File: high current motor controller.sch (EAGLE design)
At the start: 44 parts, among them Q1 IPT004N03L, Q2 IPT004N03L, Q3 IPT004N03L, Q4 IPT004N03L

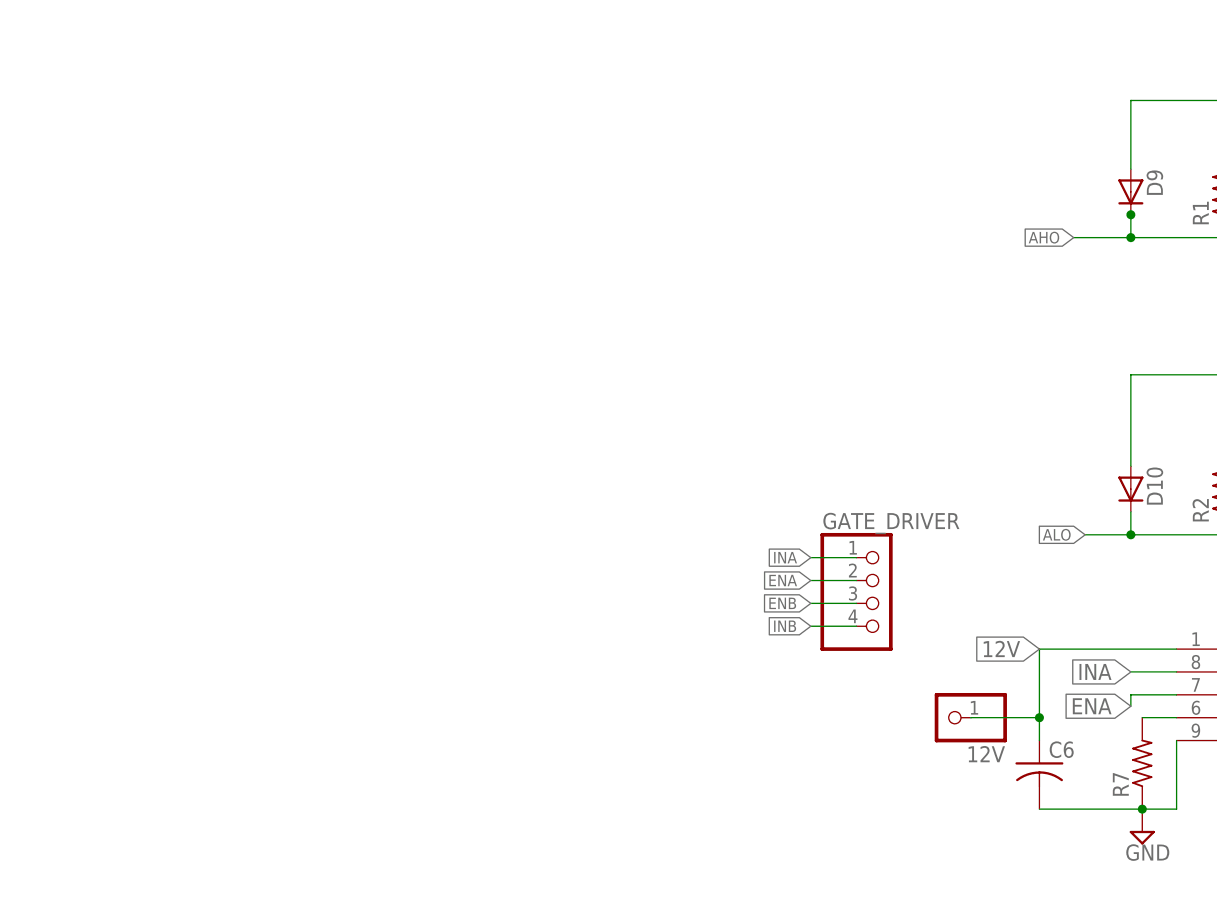
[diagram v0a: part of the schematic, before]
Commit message: Add switching regulator to transform battery voltage to 12V
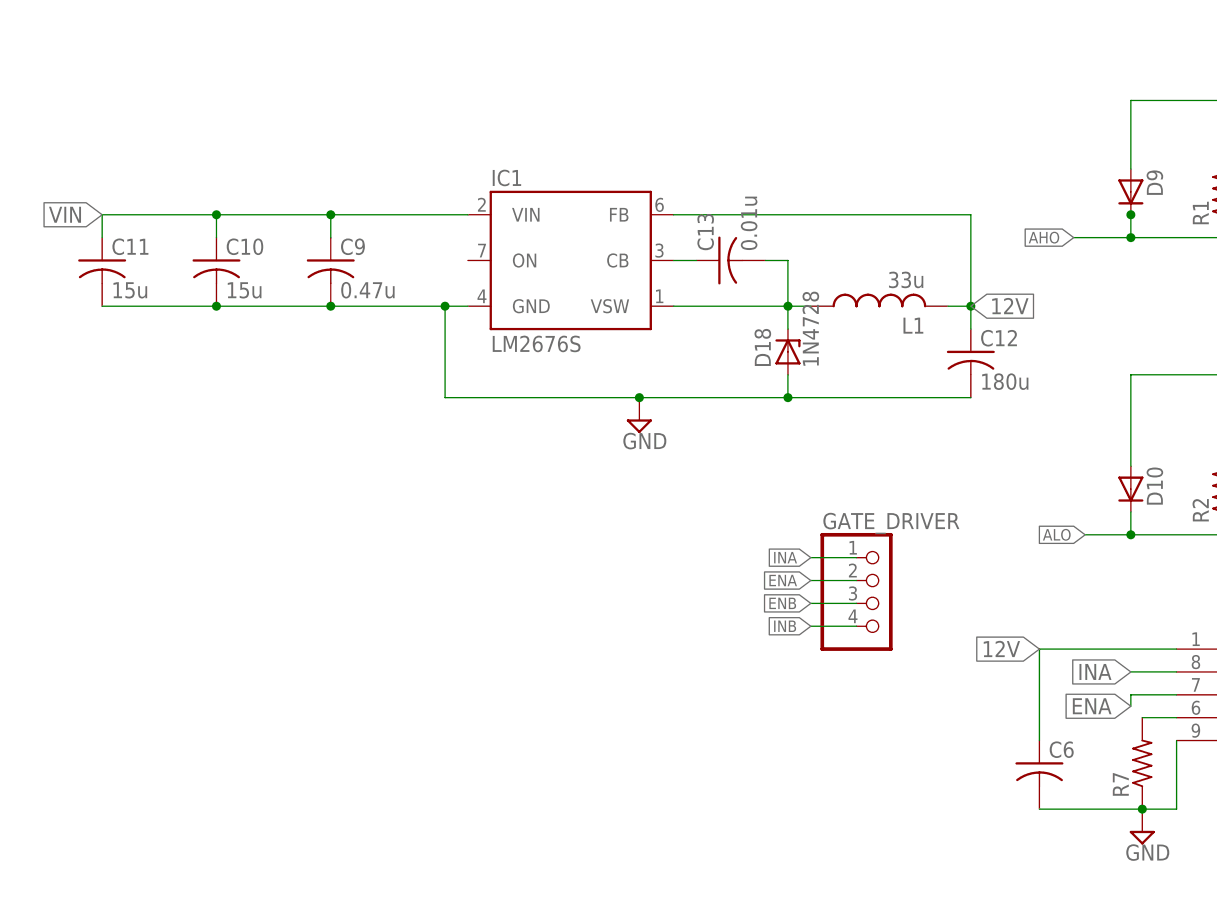
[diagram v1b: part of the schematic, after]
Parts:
- removed 12V: (no value), pinhead:PINHD-1X1
- added C10, C11: 15u, resistor:C-USC0805
- added C12: 180u, resistor:C-USC0805
- added C13: 0.01u, resistor:C-USC0805
- added C9: 0.47u, resistor:C-USC0805
- added D18: 1N4728, diode:1N4728
- added IC1: LM2676S, v-reg-3:LM2676S
- added L1: 33u, resistor:L-USL1812
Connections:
- new net N$16: C13.1, IC1.CB
- new net N$17: C13.2, D18.C, IC1.VSW, L1.1
- net 12V: now also C12.1, IC1.FB, L1.2; no longer 12V.1
- net GND: now also C10.2, C11.2, C12.2, C9.2, D18.A, IC1.GND
- net VIN: now also C10.1, C11.1, C9.1, IC1.VIN
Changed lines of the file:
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@@
 <layer number="207" name="207bmp" color="8" fill="10" visible="yes" active="yes"/>
 <layer number="208" name="208bmp" color="9" fill="10" visible="yes" active="yes"/>
+<layer number="231" name="Eagle3D_PG1" color="7" fill="1" visible="yes" active="yes"/>
+<layer number="232" name="Eagle3D_PG2" color="7" fill="1" visible="yes" active="yes"/>
+<layer number="233" name="Eagle3D_PG3" color="7" fill="1" visible="yes" active="yes"/>
 <layer number="250" name="Descript" color="3" fill="1" visible="no" active="no"/>
 <layer number="251" name="SMDround" color="12" fill="11" visible="no" active="no"/>
@@
 <part name="D17" library="diode" deviceset="GF1" device=""/>
 <part name="SUPPLY4" library="supply2" deviceset="GND" device=""/>
-<part name="12V" library="pinhead" deviceset="PINHD-1X1" device=""/>
 <part name="GATE_DRIVER" library="pinhead" deviceset="PINHD-1X4" device=""/>
 <part name="BATT_POWER" library="pinhead" deviceset="PINHD-1X3" device=""/>
+<part name="IC1" library="v-reg-3" deviceset="LM2676" device="S"/>
+<part name="C9" library="resistor" deviceset="C-US" device="C0805" value="0.47u"/>
+<part name="C10" library="resistor" deviceset="C-US" device="C0805" value="15u"/>
+<part name="C11" library="resistor" deviceset="C-US" device="C0805" value="15u"/>
+<part name="C12" library="resistor" deviceset="C-US" device="C0805" value="180u"/>
+<part name="C13" library="resistor" deviceset="C-US" device="C0805" value="0.01u"/>
+<part name="L1" library="resistor" deviceset="L-US" device="L1812" value="33u"/>
+<part name="D18" library="diode" deviceset="1N4728" device=""/>
+<part name="SUPPLY5" library="supply2" deviceset="GND" device=""/>
 </parts>
 <sheets>
@@
 <instance part="D17" gate="D" x="139.7" y="-2.54" rot="R270"/>
 <instance part="SUPPLY4" gate="GND" x="91.44" y="-27.94"/>
-<instance part="12V" gate="G$1" x="-10.16" y="-12.7" rot="R180"/>
 <instance part="GATE_DRIVER" gate="A" x="-17.78" y="0"/>
 <instance part="BATT_POWER" gate="A" x="111.76" y="78.74"/>
+<instance part="IC1" gate="A" x="-53.34" y="38.1"/>
+<instance part="C9" gate="G$1" x="-78.74" y="38.1"/>
+<instance part="C10" gate="G$1" x="-91.44" y="38.1"/>
+<instance part="C11" gate="G$1" x="-104.14" y="38.1"/>
+<instance part="C12" gate="G$1" x="-7.62" y="27.94"/>
+<instance part="C13" gate="G$1" x="-35.56" y="38.1" rot="R90"/>
+<instance part="L1" gate="G$1" x="-17.78" y="33.02" rot="R90"/>
+<instance part="D18" gate="1" x="-27.94" y="27.94" rot="R90"/>
+<instance part="SUPPLY5" gate="GND" x="-44.45" y="20.32"/>
 </instances>
 <busses>
@@
 <label x="104.14" y="76.2" size="1.27" layer="95" rot="R180" xref="yes"/>
 </segment>
+<segment>
+<pinref part="C11" gate="G$1" pin="2"/>
+<pinref part="IC1" gate="A" pin="GND"/>
+<wire x1="-104.14" y1="33.02" x2="-91.44" y2="33.02" width="0.1524" layer="91"/>
+<pinref part="C10" gate="G$1" pin="2"/>
+<wire x1="-91.44" y1="33.02" x2="-78.74" y2="33.02" width="0.1524" layer="91"/>
+<junction x="-91.44" y="33.02"/>
+<pinref part="C9" gate="G$1" pin="2"/>
+<wire x1="-78.74" y1="33.02" x2="-66.04" y2="33.02" width="0.1524" layer="91"/>
+<junction x="-78.74" y="33.02"/>
+<pinref part="C12" gate="G$1" pin="2"/>
+<wire x1="-66.04" y1="33.02" x2="-63.5" y2="33.02" width="0.1524" layer="91"/>
+<wire x1="-7.62" y1="22.86" x2="-27.94" y2="22.86" width="0.1524" layer="91"/>
+<wire x1="-27.94" y1="22.86" x2="-44.45" y2="22.86" width="0.1524" layer="91"/>
+<wire x1="-44.45" y1="22.86" x2="-66.04" y2="22.86" width="0.1524" layer="91"/>
+<wire x1="-66.04" y1="22.86" x2="-66.04" y2="33.02" width="0.1524" layer="91"/>
+<junction x="-66.04" y="33.02"/>
+<pinref part="D18" gate="1" pin="A"/>
+<wire x1="-27.94" y1="25.4" x2="-27.94" y2="22.86" width="0.1524" layer="91"/>
+<junction x="-27.94" y="22.86"/>
+<pinref part="SUPPLY5" gate="GND" pin="GND"/>
+<junction x="-44.45" y="22.86"/>
+</segment>
 </net>
 <net name="12V" class="0">
@@
 <wire x1="15.24" y1="-5.08" x2="0" y2="-5.08" width="0.1524" layer="91"/>
 <pinref part="C6" gate="G$1" pin="1"/>
-<wire x1="0" y1="-5.08" x2="0" y2="-12.7" width="0.1524" layer="91"/>
+<wire x1="0" y1="-5.08" x2="0" y2="-15.24" width="0.1524" layer="91"/>
 <label x="0" y="-5.08" size="1.778" layer="95" rot="R180" xref="yes"/>
-<pinref part="12V" gate="G$1" pin="1"/>
-<wire x1="0" y1="-12.7" x2="0" y2="-15.24" width="0.1524" layer="91"/>
-<wire x1="-7.62" y1="-12.7" x2="0" y2="-12.7" width="0.1524" layer="91"/>
-<junction x="0" y="-12.7"/>
 </segment>
 <segment>
@@
 <wire x1="139.7" y1="2.54" x2="138.43" y2="2.54" width="0.1524" layer="91"/>
 <label x="138.43" y="2.54" size="1.778" layer="95" rot="R180" xref="yes"/>
+</segment>
+<segment>
+<pinref part="L1" gate="G$1" pin="2"/>
+<pinref part="C12" gate="G$1" pin="1"/>
+<wire x1="-10.16" y1="33.02" x2="-7.62" y2="33.02" width="0.1524" layer="91"/>
+<wire x1="-7.62" y1="33.02" x2="-7.62" y2="30.48" width="0.1524" layer="91"/>
+<pinref part="IC1" gate="A" pin="FB"/>
+<wire x1="-7.62" y1="33.02" x2="-7.62" y2="43.18" width="0.1524" layer="91"/>
+<wire x1="-7.62" y1="43.18" x2="-40.64" y2="43.18" width="0.1524" layer="91"/>
+<junction x="-7.62" y="33.02"/>
+<label x="-7.62" y="33.02" size="1.778" layer="95" xref="yes"/>
 </segment>
 </net>
@@
 <label x="104.14" y="81.28" size="1.27" layer="95" rot="R180" xref="yes"/>
 </segment>
-</net>
+<segment>
+<pinref part="IC1" gate="A" pin="VIN"/>
+<pinref part="C11" gate="G$1" pin="1"/>
+<wire x1="-63.5" y1="43.18" x2="-78.74" y2="43.18" width="0.1524" layer="91"/>
+<wire x1="-78.74" y1="43.18" x2="-91.44" y2="43.18" width="0.1524" layer="91"/>
+<wire x1="-91.44" y1="43.18" x2="-104.14" y2="43.18" width="0.1524" layer="91"/>
+<wire x1="-104.14" y1="43.18" x2="-104.14" y2="40.64" width="0.1524" layer="91"/>
+<pinref part="C10" gate="G$1" pin="1"/>
+<wire x1="-91.44" y1="40.64" x2="-91.44" y2="43.18" width="0.1524" layer="91"/>
+<junction x="-91.44" y="43.18"/>
+<pinref part="C9" gate="G$1" pin="1"/>
+<wire x1="-78.74" y1="40.64" x2="-78.74" y2="43.18" width="0.1524" layer="91"/>
+<junction x="-78.74" y="43.18"/>
+<label x="-104.14" y="43.18" size="1.778" layer="95" rot="R180" xref="yes"/>
+</segment>
+</net>
+<net name="N$16" class="0">
+<segment>
+<pinref part="IC1" gate="A" pin="CB"/>
+<pinref part="C13" gate="G$1" pin="1"/>
+<wire x1="-38.1" y1="38.1" x2="-40.64" y2="38.1" width="0.1524" layer="91"/>
+</segment>
+</net>
+<net name="N$17" class="0">
+<segment>
+<pinref part="IC1" gate="A" pin="VSW"/>
+<pinref part="L1" gate="G$1" pin="1"/>
+<wire x1="-40.64" y1="33.02" x2="-27.94" y2="33.02" width="0.1524" layer="91"/>
+<pinref part="D18" gate="1" pin="C"/>
+<wire x1="-27.94" y1="33.02" x2="-25.4" y2="33.02" width="0.1524" layer="91"/>
+<wire x1="-27.94" y1="30.48" x2="-27.94" y2="33.02" width="0.1524" layer="91"/>
+<junction x="-27.94" y="33.02"/>
+<pinref part="C13" gate="G$1" pin="2"/>
+<wire x1="-27.94" y1="33.02" x2="-27.94" y2="38.1" width="0.1524" layer="91"/>
+<wire x1="-27.94" y1="38.1" x2="-30.48" y2="38.1" width="0.1524" layer="91"/>
+</segment>
+</net>

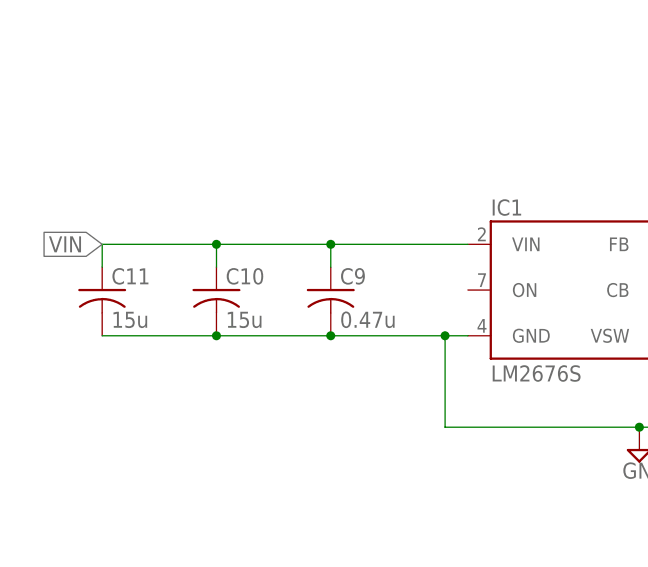
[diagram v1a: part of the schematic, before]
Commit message: Fixed regulator layout. TODO:Select values for regulator components
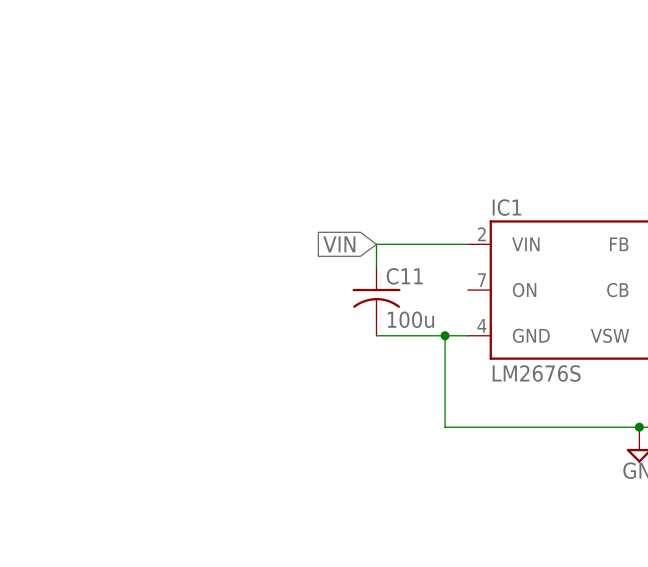
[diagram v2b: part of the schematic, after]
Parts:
- removed C10: 15u, resistor:C-USC0805
- removed C9: 0.47u, resistor:C-USC0805
- C11: value 15u -> 100u
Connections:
- net GND: no longer C10.2, C9.2
- net VIN: no longer C10.1, C9.1
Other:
- moved on the sheet: C11
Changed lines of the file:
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@@
 <part name="BATT_POWER" library="pinhead" deviceset="PINHD-1X3" device=""/>
 <part name="IC1" library="v-reg-3" deviceset="LM2676" device="S"/>
-<part name="C9" library="resistor" deviceset="C-US" device="C0805" value="0.47u"/>
-<part name="C10" library="resistor" deviceset="C-US" device="C0805" value="15u"/>
-<part name="C11" library="resistor" deviceset="C-US" device="C0805" value="15u"/>
+<part name="C11" library="resistor" deviceset="C-US" device="C0805" value="100u"/>
 <part name="C12" library="resistor" deviceset="C-US" device="C0805" value="180u"/>
 <part name="C13" library="resistor" deviceset="C-US" device="C0805" value="0.01u"/>
@@
 <instance part="BATT_POWER" gate="A" x="111.76" y="78.74"/>
 <instance part="IC1" gate="A" x="-53.34" y="38.1"/>
-<instance part="C9" gate="G$1" x="-78.74" y="38.1"/>
-<instance part="C10" gate="G$1" x="-91.44" y="38.1"/>
-<instance part="C11" gate="G$1" x="-104.14" y="38.1"/>
+<instance part="C11" gate="G$1" x="-73.66" y="38.1"/>
 <instance part="C12" gate="G$1" x="-7.62" y="27.94"/>
 <instance part="C13" gate="G$1" x="-35.56" y="38.1" rot="R90"/>
@@
 <pinref part="C11" gate="G$1" pin="2"/>
 <pinref part="IC1" gate="A" pin="GND"/>
-<wire x1="-104.14" y1="33.02" x2="-91.44" y2="33.02" width="0.1524" layer="91"/>
-<pinref part="C10" gate="G$1" pin="2"/>
-<wire x1="-91.44" y1="33.02" x2="-78.74" y2="33.02" width="0.1524" layer="91"/>
-<junction x="-91.44" y="33.02"/>
-<pinref part="C9" gate="G$1" pin="2"/>
-<wire x1="-78.74" y1="33.02" x2="-66.04" y2="33.02" width="0.1524" layer="91"/>
-<junction x="-78.74" y="33.02"/>
+<wire x1="-73.66" y1="33.02" x2="-66.04" y2="33.02" width="0.1524" layer="91"/>
 <pinref part="C12" gate="G$1" pin="2"/>
 <wire x1="-66.04" y1="33.02" x2="-63.5" y2="33.02" width="0.1524" layer="91"/>
@@
 <pinref part="IC1" gate="A" pin="VIN"/>
 <pinref part="C11" gate="G$1" pin="1"/>
-<wire x1="-63.5" y1="43.18" x2="-78.74" y2="43.18" width="0.1524" layer="91"/>
-<wire x1="-78.74" y1="43.18" x2="-91.44" y2="43.18" width="0.1524" layer="91"/>
-<wire x1="-91.44" y1="43.18" x2="-104.14" y2="43.18" width="0.1524" layer="91"/>
-<wire x1="-104.14" y1="43.18" x2="-104.14" y2="40.64" width="0.1524" layer="91"/>
-<pinref part="C10" gate="G$1" pin="1"/>
-<wire x1="-91.44" y1="40.64" x2="-91.44" y2="43.18" width="0.1524" layer="91"/>
-<junction x="-91.44" y="43.18"/>
-<pinref part="C9" gate="G$1" pin="1"/>
-<wire x1="-78.74" y1="40.64" x2="-78.74" y2="43.18" width="0.1524" layer="91"/>
-<junction x="-78.74" y="43.18"/>
-<label x="-104.14" y="43.18" size="1.778" layer="95" rot="R180" xref="yes"/>
-</segment>
-</net>
+<wire x1="-63.5" y1="43.18" x2="-73.66" y2="43.18" width="0.1524" layer="91"/>
+<wire x1="-73.66" y1="43.18" x2="-73.66" y2="40.64" width="0.1524" layer="91"/>
+<label x="-73.66" y="43.18" size="1.778" layer="95" rot="R180" xref="yes"/>
+</segment>
+</net>

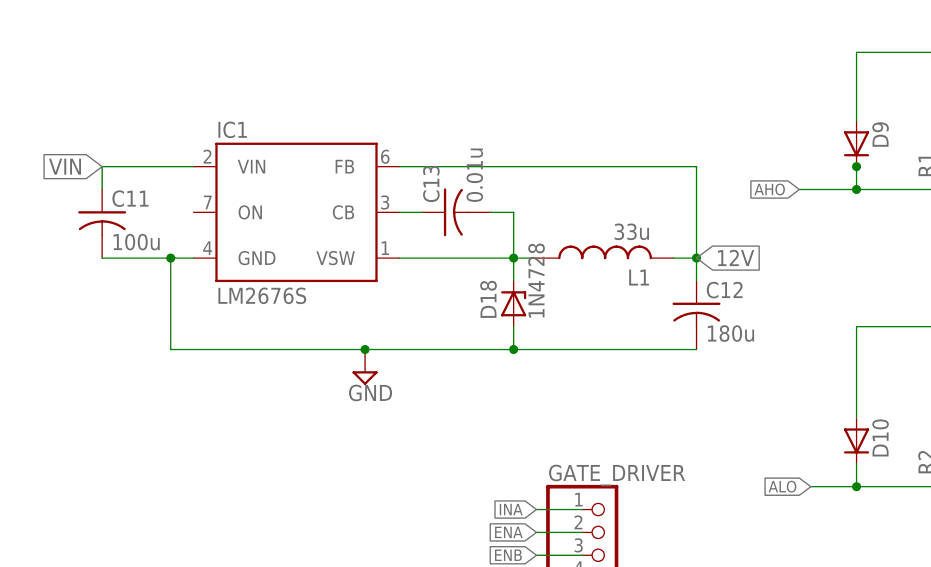
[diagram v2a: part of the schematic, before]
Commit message: Fixed silk screen overlap errors and selected values for regulator components TODO:Find corrent footprints for regulator components
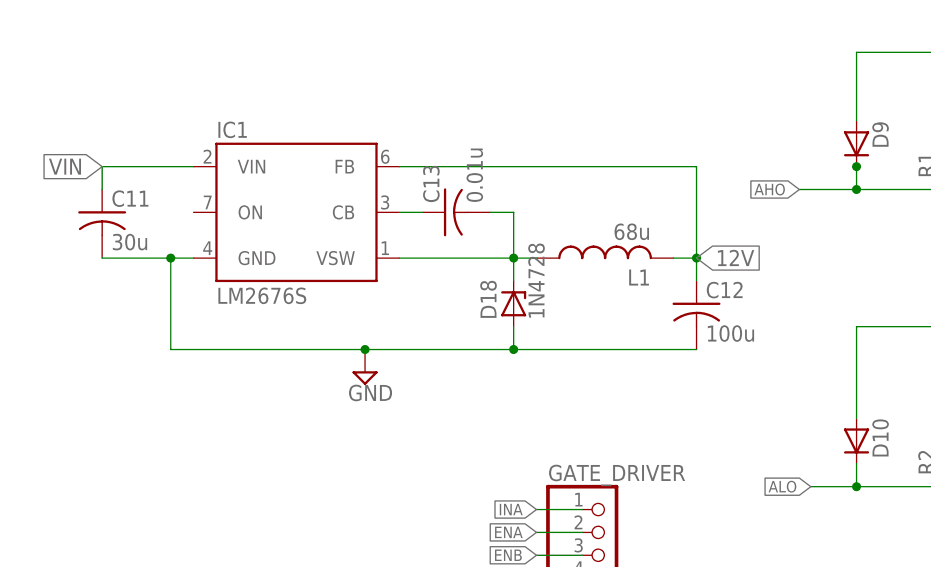
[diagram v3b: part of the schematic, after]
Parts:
- C11: value 100u -> 30u
- C12: value 180u -> 100u
- L1: value 33u -> 68u
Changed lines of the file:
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@@
 <part name="BATT_POWER" library="pinhead" deviceset="PINHD-1X3" device=""/>
 <part name="IC1" library="v-reg-3" deviceset="LM2676" device="S"/>
-<part name="C11" library="resistor" deviceset="C-US" device="C0805" value="100u"/>
-<part name="C12" library="resistor" deviceset="C-US" device="C0805" value="180u"/>
+<part name="C11" library="resistor" deviceset="C-US" device="C0805" value="30u"/>
+<part name="C12" library="resistor" deviceset="C-US" device="C0805" value="100u"/>
 <part name="C13" library="resistor" deviceset="C-US" device="C0805" value="0.01u"/>
-<part name="L1" library="resistor" deviceset="L-US" device="L1812" value="33u"/>
+<part name="L1" library="resistor" deviceset="L-US" device="L1812" value="68u"/>
 <part name="D18" library="diode" deviceset="1N4728" device=""/>
 <part name="SUPPLY5" library="supply2" deviceset="GND" device=""/>
